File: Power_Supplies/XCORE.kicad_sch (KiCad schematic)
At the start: 7 parts, among them U10 XU316-1024-TQ128-I24, U11 W25Q64JVSSIQ (FLASH MEMORY), X1 FA-238 24.0000MB-C0 (CRYSTAL)

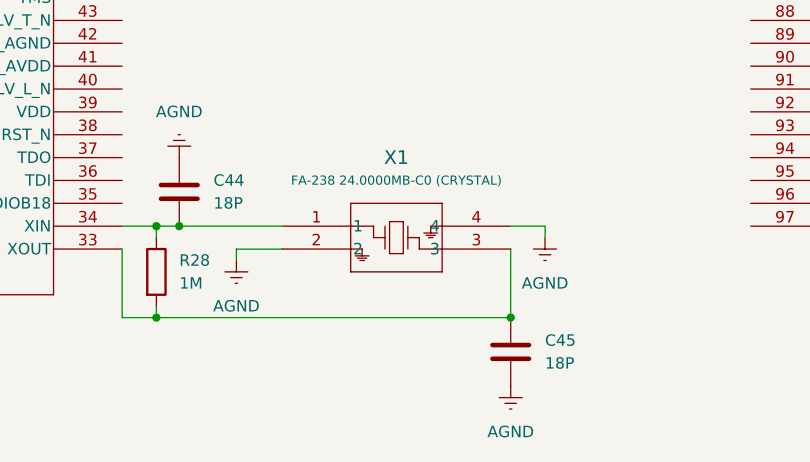
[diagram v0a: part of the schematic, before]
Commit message: Added Phantom Power, updated Xcore library things
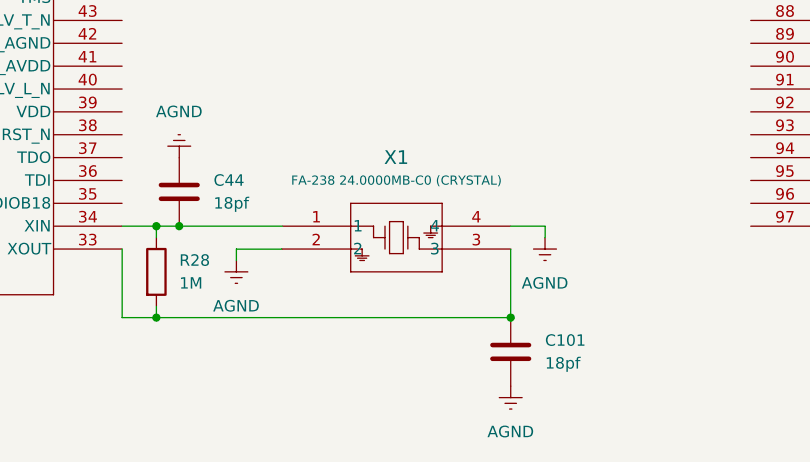
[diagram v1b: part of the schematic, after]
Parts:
- C101: renamed from C45; value 18P -> 18pf
- C44: value 18P -> 18pf
- U10: footprint TQFP128_196X196_XMO -> SamacSys_Parts:TQFP128_196X196_XMO
- U11: footprint SOIC-8_5P28X5P28_WIN -> SamacSys_Parts:SOIC-8_5P28X5P28_WIN
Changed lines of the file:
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@@
+	(wire
+		(pts
+			(xy 109.22 29.21) (xy 114.3 29.21)
+		)
+		(stroke
+			(width 0)
+			(type default)
+		)
+	)
+	(wire
+		(pts
+			(xy 55.88 69.85) (xy 53.34 69.85)
+		)
+		(stroke
+			(width 0)
+			(type default)
+		)
+	)
+	(wire
+		(pts
+			(xy 199.39 29.21) (xy 205.74 29.21)
+		)
+		(stroke
+			(width 0)
+			(type default)
+		)
+	)
+	(wire
+		(pts
+			(xy 195.58 39.37) (xy 199.39 39.37)
+		)
+		(stroke
+			(width 0)
+			(type default)
+		)
+	)
+	(wire
+		(pts
+			(xy 125.73 140.97) (xy 125.73 142.24)
+		)
+		(stroke
+			(width 0)
+			(type default)
+		)
+	)
+	(wire
+		(pts
+			(xy 203.2 38.1) (xy 205.74 38.1)
+		)
+		(stroke
+			(width 0)
+			(type default)
+		)
+	)
+	(wire
+		(pts
+			(xy 247.65 62.23) (xy 247.65 64.77)
+		)
+		(stroke
+			(width 0)
+			(type default)
+		)
+	)
+	(wire
+		(pts
+			(xy 50.8 59.69) (xy 50.8 62.23)
+		)
+		(stroke
+			(width 0)
+			(type default)
+		)
+	)
+	(wire
+		(pts
+			(xy 49.53 74.93) (xy 46.99 74.93)
+		)
+		(stroke
+			(width 0)
+			(type default)
+		)
+	)
+	(wire
+		(pts
+			(xy 50.8 69.85) (xy 50.8 67.31)
+		)
+		(stroke
+			(width 0)
+			(type default)
+		)
+	)
+	(wire
+		(pts
+			(xy 195.58 31.75) (xy 199.39 31.75)
+		)
+		(stroke
+			(width 0)
+			(type default)
+		)
+	)
 	(wire
 		(pts
@@
 	(wire
 		(pts
-			(xy 109.22 29.21) (xy 114.3 29.21)
-		)
-		(stroke
-			(width 0)
-			(type default)
-		)
-	)
-	(wire
-		(pts
-			(xy 55.88 69.85) (xy 53.34 69.85)
-		)
-		(stroke
-			(width 0)
-			(type default)
-		)
-	)
-	(wire
-		(pts
-			(xy 199.39 29.21) (xy 205.74 29.21)
-		)
-		(stroke
-			(width 0)
-			(type default)
-		)
-	)
-	(wire
-		(pts
-			(xy 195.58 39.37) (xy 199.39 39.37)
-		)
-		(stroke
-			(width 0)
-			(type default)
-		)
-	)
-	(wire
-		(pts
-			(xy 125.73 140.97) (xy 125.73 142.24)
-		)
-		(stroke
-			(width 0)
-			(type default)
-		)
-	)
-	(wire
-		(pts
-			(xy 203.2 38.1) (xy 205.74 38.1)
-		)
-		(stroke
-			(width 0)
-			(type default)
-		)
-	)
-	(wire
-		(pts
-			(xy 247.65 62.23) (xy 247.65 64.77)
-		)
-		(stroke
-			(width 0)
-			(type default)
-		)
-	)
-	(wire
-		(pts
-			(xy 50.8 59.69) (xy 50.8 62.23)
-		)
-		(stroke
-			(width 0)
-			(type default)
-		)
-	)
-	(wire
-		(pts
-			(xy 49.53 74.93) (xy 46.99 74.93)
-		)
-		(stroke
-			(width 0)
-			(type default)
-		)
-	)
-	(wire
-		(pts
-			(xy 50.8 69.85) (xy 50.8 67.31)
-		)
-		(stroke
-			(width 0)
-			(type default)
-		)
-	)
-	(wire
-		(pts
-			(xy 195.58 31.75) (xy 199.39 31.75)
-		)
-		(stroke
-			(width 0)
-			(type default)
-		)
-	)
-	(wire
-		(pts
 			(xy 165.1 140.97) (xy 168.91 140.97)
 		)
@@
 	(wire
 		(pts
+			(xy 199.39 39.37) (xy 199.39 43.18)
+		)
+		(stroke
+			(width 0)
+			(type default)
+		)
+	)
+	(wire
+		(pts
 			(xy 195.58 36.83) (xy 203.2 36.83)
 		)
@@
 		(pts
 			(xy 106.68 24.13) (xy 109.22 24.13)
-		)
-		(stroke
-			(width 0)
-			(type default)
-		)
-	)
-	(wire
-		(pts
-			(xy 199.39 39.37) (xy 199.39 43.18)
 		)
 		(stroke
@@
 		(instances
 			(project ""
-				(path "/5266cf9e-da90-4c53-80fd-cf3dbed42632/2c89b534-1f3e-4e8b-9c0c-c669faa35136"
+				(path "/5266cf9e-da90-4c53-80fd-cf3dbed42632/4ac374da-48c1-45fc-82eb-58af98bfd6f4"
 					(reference "X1")
 					(unit 1)
@@
 		(dnp no)
 		(fields_autoplaced yes)
-		(property "Reference" "#PWR038"
+		(property "Reference" "#PWR0101"
 			(at 114.3 48.26 0)
 			(effects
@@
 		(instances
 			(project "Power_Supplies"
-				(path "/5266cf9e-da90-4c53-80fd-cf3dbed42632/2c89b534-1f3e-4e8b-9c0c-c669faa35136"
-					(reference "#PWR038")
+				(path "/5266cf9e-da90-4c53-80fd-cf3dbed42632/4ac374da-48c1-45fc-82eb-58af98bfd6f4"
+					(reference "#PWR0101")
 					(unit 1)
 				)
@@
 		(dnp no)
 		(fields_autoplaced yes)
-		(property "Reference" "#PWR037"
+		(property "Reference" "#PWR0102"
 			(at 165.1 165.1 0)
 			(effects
@@
 		(instances
 			(project "Power_Supplies"
-				(path "/5266cf9e-da90-4c53-80fd-cf3dbed42632/2c89b534-1f3e-4e8b-9c0c-c669faa35136"
-					(reference "#PWR037")
+				(path "/5266cf9e-da90-4c53-80fd-cf3dbed42632/4ac374da-48c1-45fc-82eb-58af98bfd6f4"
+					(reference "#PWR0102")
 					(unit 1)
 				)
@@
 			)
 		)
-		(property "Footprint" "SOIC-8_5P28X5P28_WIN"
+		(property "Footprint" "SamacSys_Parts:SOIC-8_5P28X5P28_WIN"
 			(at 114.3 31.75 0)
 			(effects
@@
 		(instances
 			(project ""
-				(path "/5266cf9e-da90-4c53-80fd-cf3dbed42632/2c89b534-1f3e-4e8b-9c0c-c669faa35136"
+				(path "/5266cf9e-da90-4c53-80fd-cf3dbed42632/4ac374da-48c1-45fc-82eb-58af98bfd6f4"
 					(reference "U11")
 					(unit 1)
@@
 		(instances
 			(project ""
-				(path "/5266cf9e-da90-4c53-80fd-cf3dbed42632/2c89b534-1f3e-4e8b-9c0c-c669faa35136"
-					(reference "#PWR035")
+				(path "/5266cf9e-da90-4c53-80fd-cf3dbed42632/4ac374da-48c1-45fc-82eb-58af98bfd6f4"
+					(reference "#PWR0104")
 					(unit 1)
 				)
@@
 		(instances
 			(project ""
-				(path "/5266cf9e-da90-4c53-80fd-cf3dbed42632/2c89b534-1f3e-4e8b-9c0c-c669faa35136"
+				(path "/5266cf9e-da90-4c53-80fd-cf3dbed42632/4ac374da-48c1-45fc-82eb-58af98bfd6f4"
 					(reference "R29")
 					(unit 1)
@@
 			)
 		)
-		(property "Value" "18P"
+		(property "Value" "18pf"
 			(at 132.08 138.4299 0)
 			(effects
@@
 		(instances
 			(project ""
-				(path "/5266cf9e-da90-4c53-80fd-cf3dbed42632/2c89b534-1f3e-4e8b-9c0c-c669faa35136"
-					(reference "C44")
+				(path "/5266cf9e-da90-4c53-80fd-cf3dbed42632/4ac374da-48c1-45fc-82eb-58af98bfd6f4"
+					(reference "C100")
 					(unit 1)
 				)
@@
 		(instances
 			(project ""
-				(path "/5266cf9e-da90-4c53-80fd-cf3dbed42632/2c89b534-1f3e-4e8b-9c0c-c669faa35136"
+				(path "/5266cf9e-da90-4c53-80fd-cf3dbed42632/4ac374da-48c1-45fc-82eb-58af98bfd6f4"
 					(reference "R28")
 					(unit 1)
@@
 		(instances
 			(project ""
-				(path "/5266cf9e-da90-4c53-80fd-cf3dbed42632/2c89b534-1f3e-4e8b-9c0c-c669faa35136"
-					(reference "#PWR034")
+				(path "/5266cf9e-da90-4c53-80fd-cf3dbed42632/4ac374da-48c1-45fc-82eb-58af98bfd6f4"
+					(reference "#PWR0103")
 					(unit 1)
 				)
@@
 			)
 		)
-		(property "Footprint" "TQFP128_196X196_XMO"
+		(property "Footprint" "SamacSys_Parts:TQFP128_196X196_XMO"
 			(at 55.88 62.23 0)
 			(effects
@@
 		(instances
 			(project ""
-				(path "/5266cf9e-da90-4c53-80fd-cf3dbed42632/2c89b534-1f3e-4e8b-9c0c-c669faa35136"
+				(path "/5266cf9e-da90-4c53-80fd-cf3dbed42632/4ac374da-48c1-45fc-82eb-58af98bfd6f4"
 					(reference "U10")
 					(unit 1)
@@
 		(instances
 			(project ""
-				(path "/5266cf9e-da90-4c53-80fd-cf3dbed42632/2c89b534-1f3e-4e8b-9c0c-c669faa35136"
-					(reference "#PWR036")
+				(path "/5266cf9e-da90-4c53-80fd-cf3dbed42632/4ac374da-48c1-45fc-82eb-58af98bfd6f4"
+					(reference "#PWR0105")
 					(unit 1)
 				)
@@
 			)
 		)
-		(property "Footprint" "TQFP128_196X196_XMO"
+		(property "Footprint" "SamacSys_Parts:TQFP128_196X196_XMO"
 			(at 191.77 62.23 0)
 			(effects
@@
 		(instances
 			(project ""
-				(path "/5266cf9e-da90-4c53-80fd-cf3dbed42632/2c89b534-1f3e-4e8b-9c0c-c669faa35136"
+				(path "/5266cf9e-da90-4c53-80fd-cf3dbed42632/4ac374da-48c1-45fc-82eb-58af98bfd6f4"
 					(reference "U10")
 					(unit 2)
@@
 		(dnp no)
 		(fields_autoplaced yes)
-		(property "Reference" "C45"
+		(property "Reference" "C101"
 			(at 168.91 153.6699 0)
 			(effects
@@
 			)
 		)
-		(property "Value" "18P"
+		(property "Value" "18pf"
 			(at 168.91 156.2099 0)
 			(effects
@@
 		(instances
 			(project "Power_Supplies"
-				(path "/5266cf9e-da90-4c53-80fd-cf3dbed42632/2c89b534-1f3e-4e8b-9c0c-c669faa35136"
-					(reference "C45")
+				(path "/5266cf9e-da90-4c53-80fd-cf3dbed42632/4ac374da-48c1-45fc-82eb-58af98bfd6f4"
+					(reference "C101")
 					(unit 1)
 				)

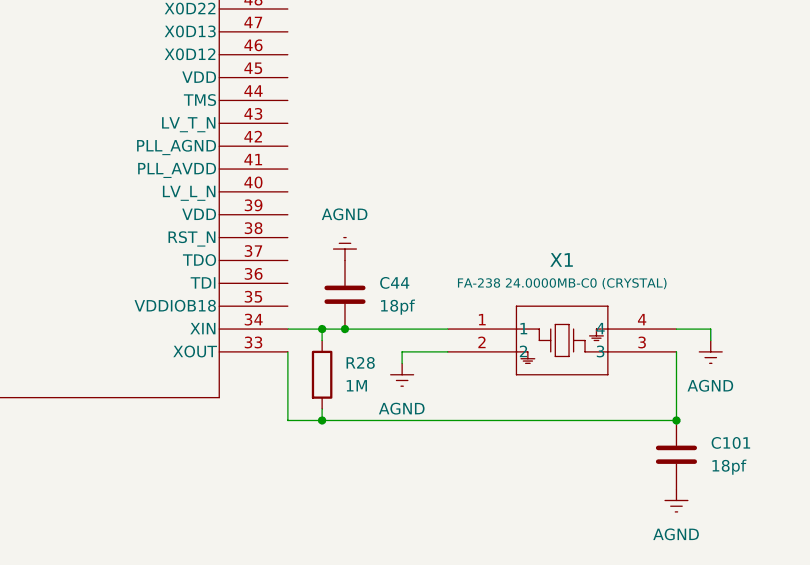
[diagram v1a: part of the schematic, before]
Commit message: Started preamp design (finished stage 1)
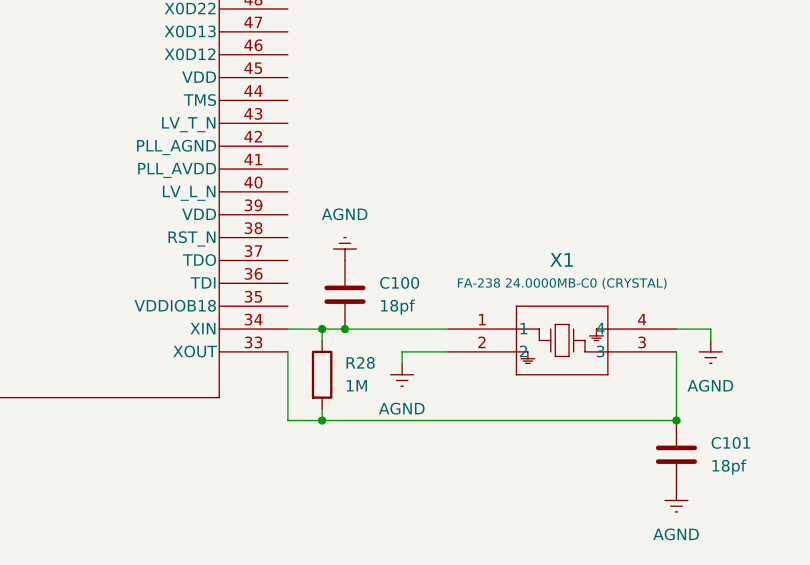
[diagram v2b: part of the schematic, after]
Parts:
- renumbered C44 to C100
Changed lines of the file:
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@@
 		(dnp no)
 		(fields_autoplaced yes)
-		(property "Reference" "#PWR035"
+		(property "Reference" "#PWR0104"
 			(at 134.62 151.13 0)
 			(effects
@@
 		(dnp no)
 		(fields_autoplaced yes)
-		(property "Reference" "C44"
+		(property "Reference" "C100"
 			(at 132.08 135.8899 0)
 			(effects
@@
 		(dnp no)
 		(fields_autoplaced yes)
-		(property "Reference" "#PWR034"
+		(property "Reference" "#PWR0103"
 			(at 168.91 148.59 0)
 			(effects
@@
 		(dnp no)
 		(fields_autoplaced yes)
-		(property "Reference" "#PWR036"
+		(property "Reference" "#PWR0105"
 			(at 128.27 127 0)
 			(effects
